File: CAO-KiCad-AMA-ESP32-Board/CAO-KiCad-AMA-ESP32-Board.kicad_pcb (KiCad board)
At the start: 2 copper layers, 100 x 69 mm, 112 parts, among them J13 DHT Sensor, J14 Pot, J15 Select A, J16 Select B, J17 I2C, J3 Conn_01x19, J4 Conn_01x19, J5 Micro_SD_Card, J6 Servo, J7 I2C, J8 5V Ext, Q1 IRLML6402, SW1 SW_Push, SW2 SW_Push, SW3 SW_Push, SW4 SW_Push, SW5 SW_Push, SW6 SW_Push, U1 ESP32-DevKitC, U2 74HC595, Y1 Crystal_GND3_Small

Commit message: Ajout du schématique et de la BOM
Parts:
- C12: value 10u -> DNP
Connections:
- net /SW Digital renamed /Digital_SW

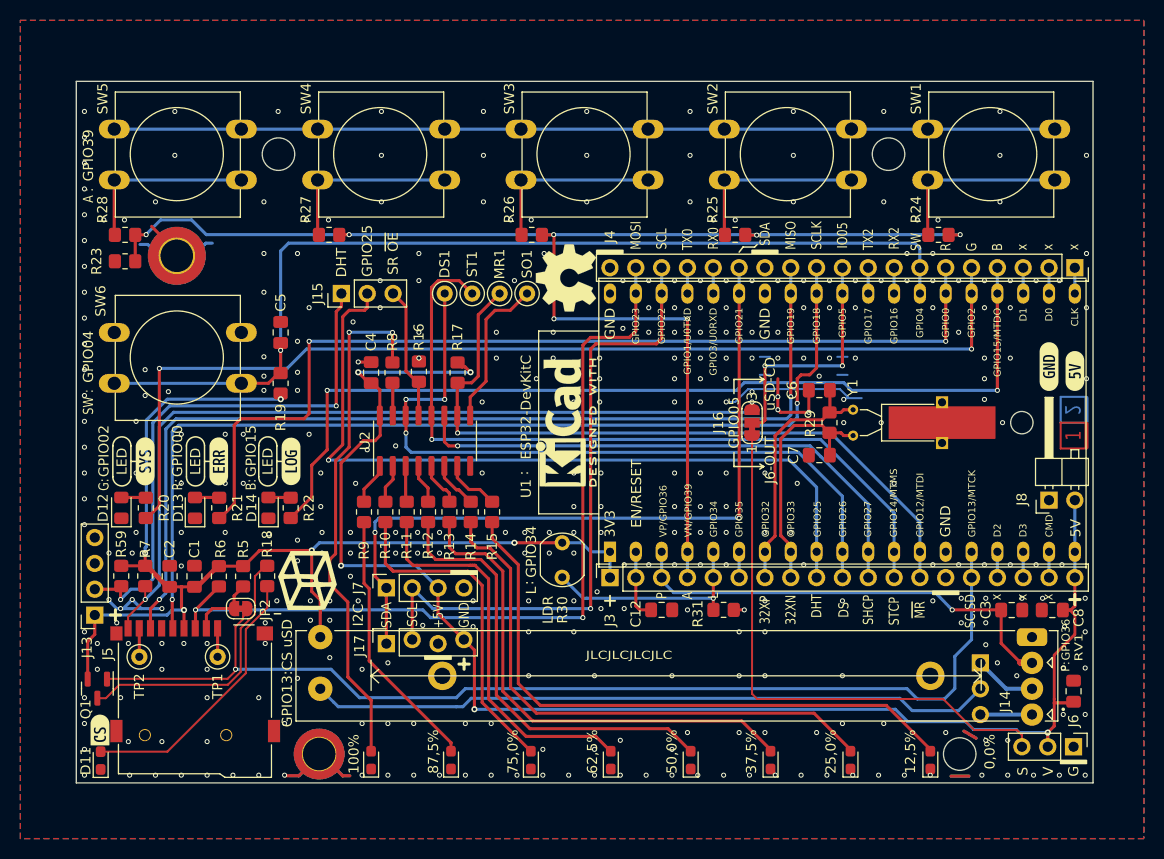
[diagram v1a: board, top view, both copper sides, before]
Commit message: Correction majeur sur le GPIO12, doit-être à l'état bas lors du démarrage de l'ESP32
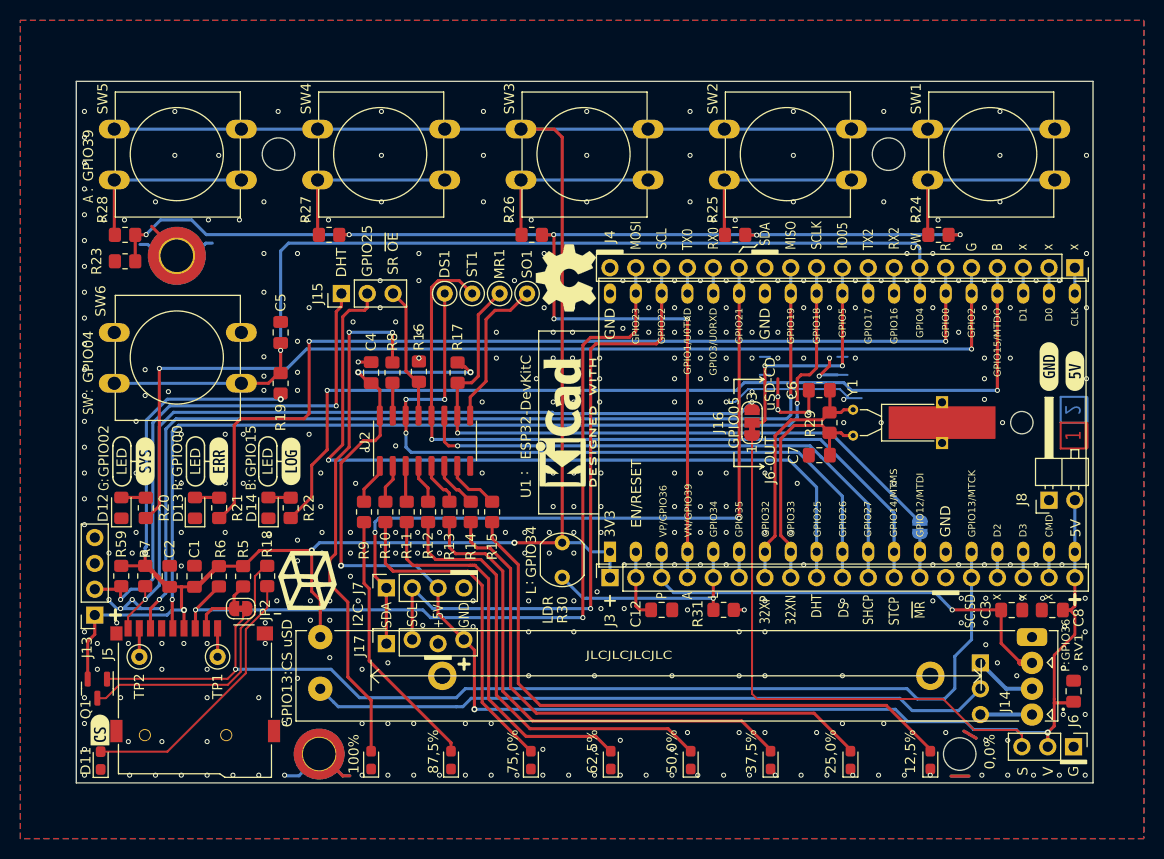
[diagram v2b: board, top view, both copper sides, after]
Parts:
- added JP1: Jumper_2_Open, Jumper:SolderJumper-2_P1.3mm_Open_RoundedPad1.0x1.5mm, B.Cu at (173.0, 109.9)
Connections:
- J3 pad 13: /SR MR -> /GPIO12
- U1 pad 13: /SR MR -> /GPIO12
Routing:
- net +3V3: track 210.0 -> 254.1 mm
- net /SR MR: track 70.8 -> 65.4 mm
- net /GPIO12: track 0.00 -> 4.18 mm
- net GND: track 72.4 -> 72.6 mm, vias 357 -> 367

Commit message: MAJ valeurs R pour LEDs
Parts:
- D11, D14: value LED -> BLUE
- D12: value LED -> GREEN
- D13: value LED -> RED
- R10, R11, R12, R13, R14, R15, R21, R8, R9: value 560 -> 1k
- R20: value 560 -> 1k2
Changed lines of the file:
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@@
       (effects (font (size 1 1) (thickness 0.15)))
     )
-    (fp_text value "LED" (at 0 1.65 90) (layer "F.Fab")
+    (fp_text value "BLUE" (at 0 1.65 90) (layer "F.Fab")
       (effects (font (size 1 1) (thickness 0.15)))
     )
@@
       (effects (font (size 1 1) (thickness 0.15)))
     )
-    (fp_text value "560" (at 2.775 0.068834 90) (layer "F.Fab")
+    (fp_text value "1k" (at 2.775 0.068834 90) (layer "F.Fab")
       (effects (font (size 1 1) (thickness 0.15)))
     )
@@
       (effects (font (size 1 1) (thickness 0.15)))
     )
-    (fp_text value "560" (at 0 1.65 90) (layer "F.Fab")
+    (fp_text value "1k" (at 0 1.65 90) (layer "F.Fab")
       (effects (font (size 1 1) (thickness 0.15)))
     )
@@
       (effects (font (size 1 1) (thickness 0.15)))
     )
-    (fp_text value "LED" (at 0 1.43 90) (layer "F.Fab")
+    (fp_text value "BLUE" (at 0 1.43 90) (layer "F.Fab")
       (effects (font (size 1 1) (thickness 0.15)))
     )
@@
       (effects (font (size 1 1) (thickness 0.15)))
     )
-    (fp_text value "560" (at 2.775 -0.01583 90) (layer "F.Fab")
+    (fp_text value "1k" (at 2.775 -0.01583 90) (layer "F.Fab")
       (effects (font (size 1 1) (thickness 0.15)))
     )
@@
       (effects (font (size 1 1) (thickness 0.15)))
     )
-    (fp_text value "560" (at 2.775 0.005336 90) (layer "F.Fab")
+    (fp_text value "1k" (at 2.775 0.005336 90) (layer "F.Fab")
       (effects (font (size 1 1) (thickness 0.15)))
     )
@@
       (effects (font (size 1 1) (thickness 0.15)))
     )
-    (fp_text value "LED" (at 0 1.65 90) (layer "F.Fab")
+    (fp_text value "RED" (at 0 1.65 90) (layer "F.Fab")
       (effects (font (size 1 1) (thickness 0.15)))
     )
@@
       (effects (font (size 1 1) (thickness 0.15)))
     )
-    (fp_text value "560" (at 2.775 0.026502 90) (layer "F.Fab")
+    (fp_text value "1k" (at 2.775 0.026502 90) (layer "F.Fab")
       (effects (font (size 1 1) (thickness 0.15)))
     )
@@
       (effects (font (size 1 1) (thickness 0.15)))
     )
-    (fp_text value "560" (at 0 1.65 90) (layer "F.Fab")
+    (fp_text value "1k" (at 0 1.65 90) (layer "F.Fab")
       (effects (font (size 1 1) (thickness 0.15)))
     )
@@
       (effects (font (size 1 1) (thickness 0.15)))
     )
-    (fp_text value "LED" (at 0 1.65 90) (layer "F.Fab")
+    (fp_text value "GREEN" (at 0 1.65 90) (layer "F.Fab")
       (effects (font (size 1 1) (thickness 0.15)))
     )
@@
       (effects (font (size 1 1) (thickness 0.15)))
     )
-    (fp_text value "560" (at 2.775 -0.037 90) (layer "F.Fab")
+    (fp_text value "1k" (at 2.775 -0.037 90) (layer "F.Fab")
       (effects (font (size 1 1) (thickness 0.15)))
     )
@@
       (effects (font (size 1 1) (thickness 0.15)))
     )
-    (fp_text value "560" (at 2.775 0.047668 90) (layer "F.Fab")
+    (fp_text value "1k" (at 2.775 0.047668 90) (layer "F.Fab")
       (effects (font (size 1 1) (thickness 0.15)))
     )
@@
       (effects (font (size 1 1) (thickness 0.15)))
     )
-    (fp_text value "560" (at 2.775 0.09 90) (layer "F.Fab")
+    (fp_text value "1k" (at 2.775 0.09 90) (layer "F.Fab")
       (effects (font (size 1 1) (thickness 0.15)))
     )
@@
       (effects (font (size 1 1) (thickness 0.15)))
     )
-    (fp_text value "560" (at 0 1.65 90) (layer "F.Fab")
+    (fp_text value "1k2" (at 0 1.65 90) (layer "F.Fab")
       (effects (font (size 1 1) (thickness 0.15)))
     )
